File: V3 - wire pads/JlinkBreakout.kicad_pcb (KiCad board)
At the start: 2 copper layers, 38.5 x 27 mm, 11 parts, among them J1 JLINK, J2 TC, J3 SWD, U1 SGM2019, U2 switch_0204

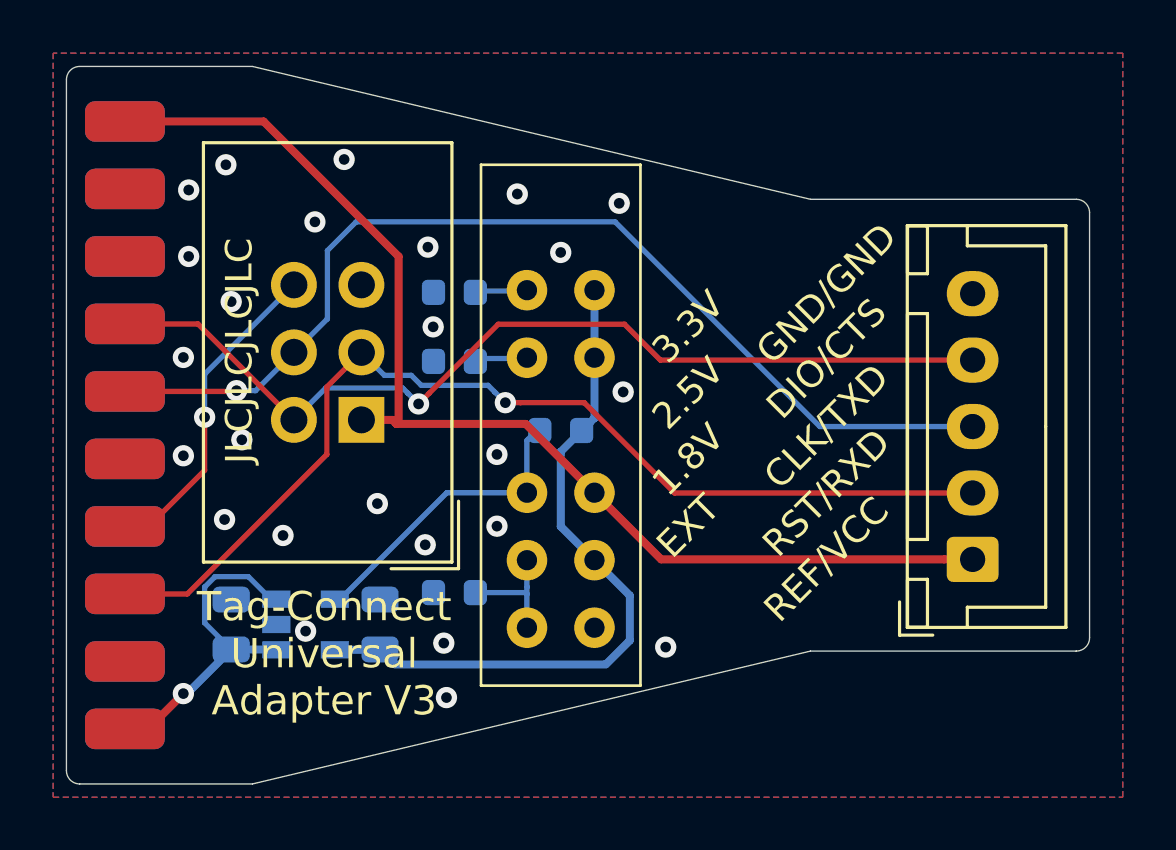
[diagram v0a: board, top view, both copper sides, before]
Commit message: Route v3-wire pads PCB, add to README
Uses solder jumpers to select voltage, external power input/output pads
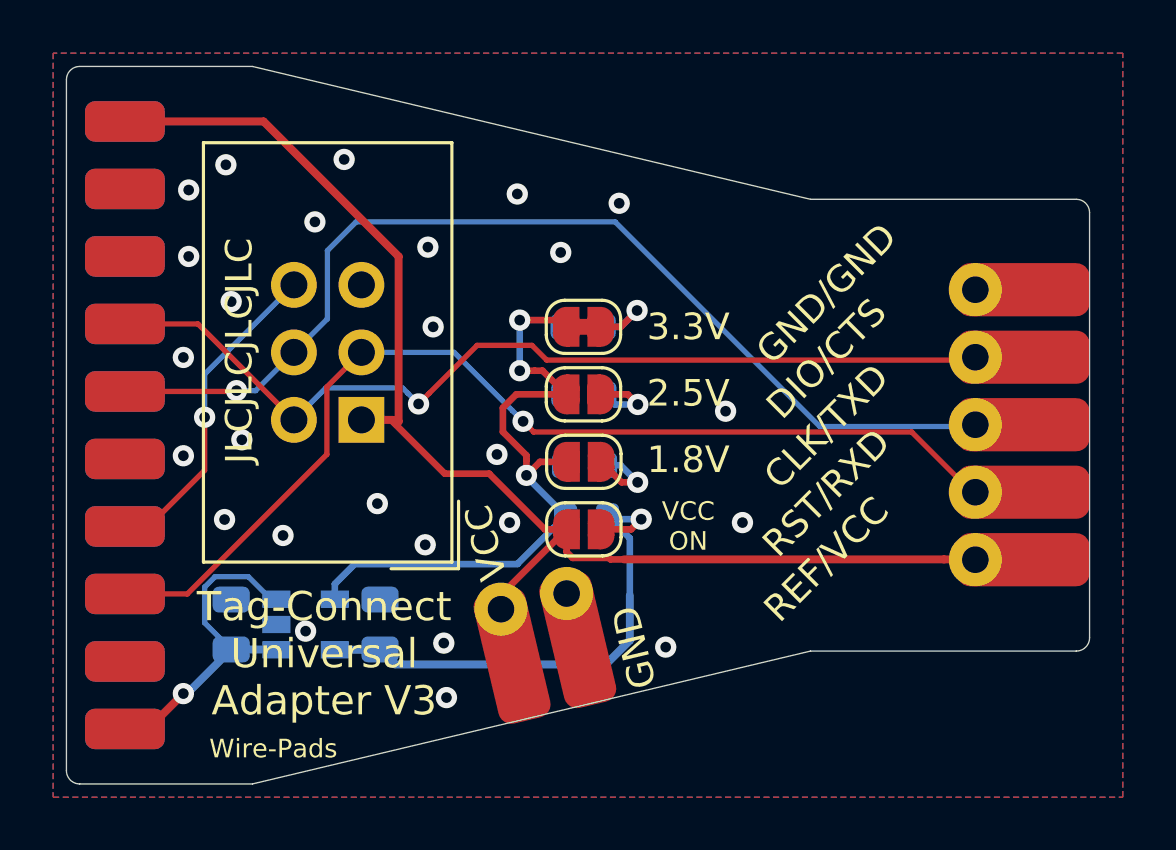
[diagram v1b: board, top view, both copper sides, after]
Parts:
- removed U2: switch_0204, otter:SS-24E06-TG
- added J4: PWR_IN, 0 - GIE Connectors, Terminal Blocks:conn_edge_PTH_2.54mm_2x5_02, F.Cu at (75.8, 54.1)
- added JP1: Vreg_3.3V, Jumper:SolderJumper-2_P1.3mm_Bridged_RoundedPad1.0x1.5mm, F.Cu at (77.5, 42.8)
- added JP2: Vreg_2.5V, Jumper:SolderJumper-2_P1.3mm_Open_RoundedPad1.0x1.5mm, F.Cu at (77.5, 45.3)
- added JP3: Vreg_1.8V, Jumper:SolderJumper-2_P1.3mm_Open_RoundedPad1.0x1.5mm, F.Cu at (77.5, 47.9)
- added JP4: Vreg_to_Vtref, Jumper:SolderJumper-2_P1.3mm_Open_RoundedPad1.0x1.5mm, F.Cu at (77.5, 50.4)
- C1, C2: value 1u -> 2.2u
- J3: footprint Connector_JST:JST_XH_B5B-XH-A_1x05_P2.50mm_Vertical -> 0 - GIE Connectors, Terminal Blocks:conn_edge_PTH_2.54mm_2x5_05
- R1: value 10k -> 10k 1%
- R2: value 17.5k -> 20k 1%
- R3: value 10.8k -> 9.31k 1%
- R4: value 5k -> 5.76k 1%
- moved R2 11.1 mm to (77.4, 42.8)
- moved R4 8.14 mm to (77.5, 48.0)
- moved J3 5.19 mm to (93.2, 46.5)
- moved R3 5.03 mm to (77.5, 45.3)
- moved R1 3.35 mm to (77.6, 49.9)
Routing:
- net Net-(JP1-Pad1): track 11.5 -> 25.8 mm, vias 0 -> 3
- net LDOOUT: track 26.5 -> 19.7 mm, vias 0 -> 1
- net REF: track 43.9 -> 49.8 mm
- net Net-(JP3-Pad2): track 1.96 -> 3.17 mm, vias 0 -> 1
- net Net-(JP1-Pad2): track 4.50 -> 3.39 mm, vias 0 -> 1
- net Net-(JP2-Pad2): track 1.99 -> 2.96 mm, vias 0 -> 1
- net DIO: track 35.9 -> 35.3 mm
- net GND: vias 25 -> 26
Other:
- board text added: "GND"
- board text added: "VCC"
- board text added: "VCC ON"
- board text added: "Wire-Pads"
- board text removed: "EXT"
